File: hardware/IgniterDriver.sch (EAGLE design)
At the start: 51 parts, among them IC1 4066D, T3 TJ8S06M3L(T6L1,NQ)

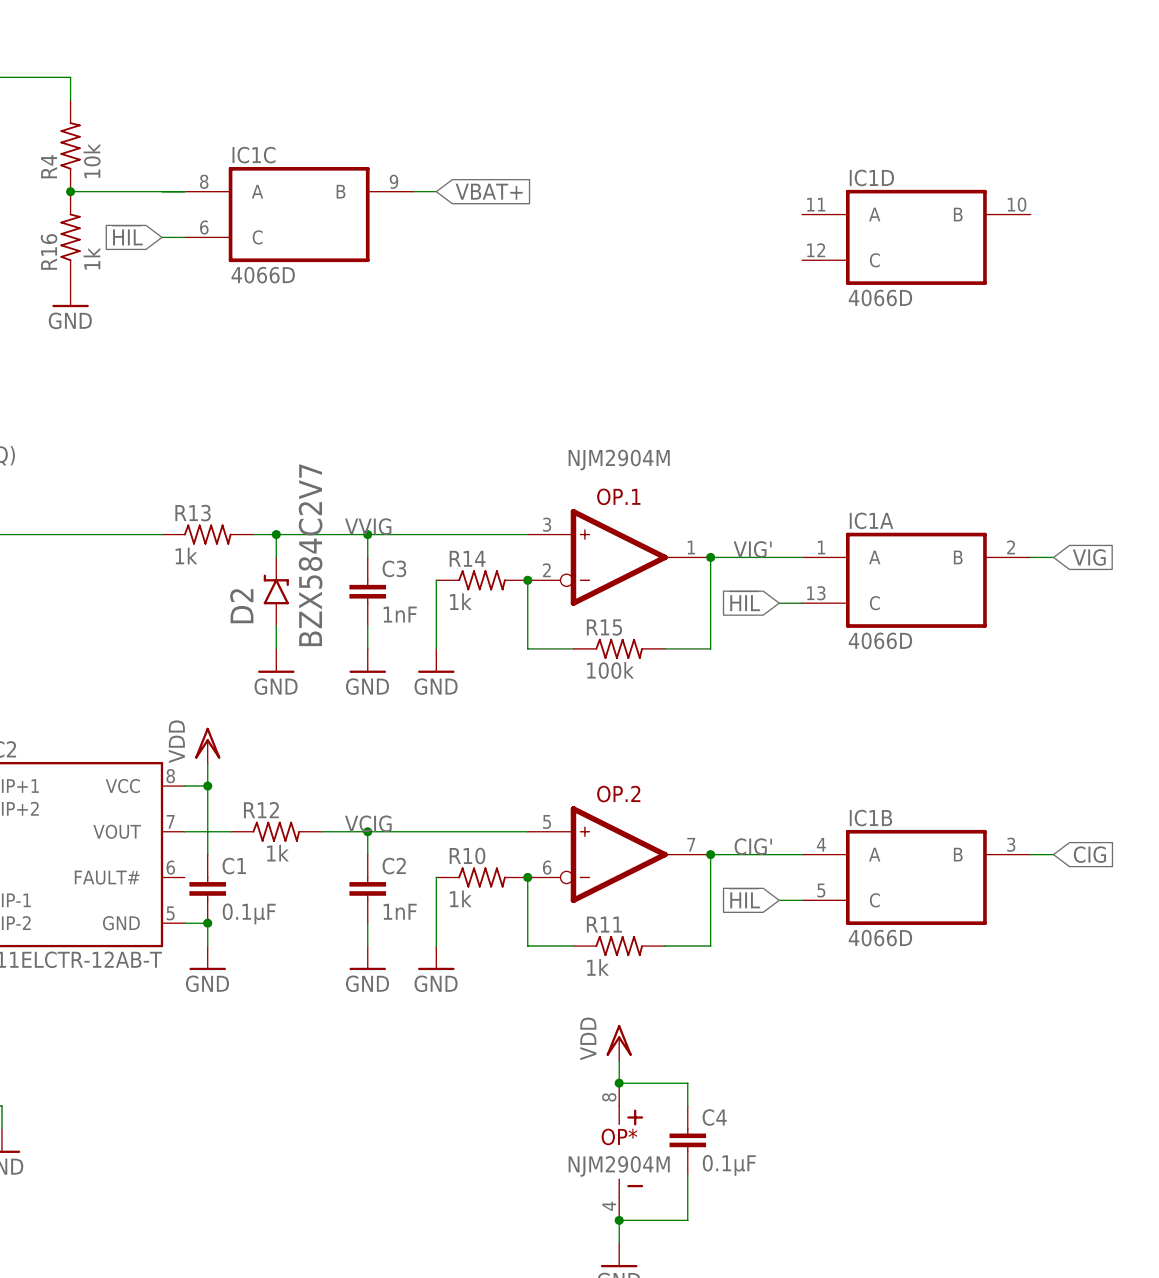
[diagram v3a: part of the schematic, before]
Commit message: Clean silk print
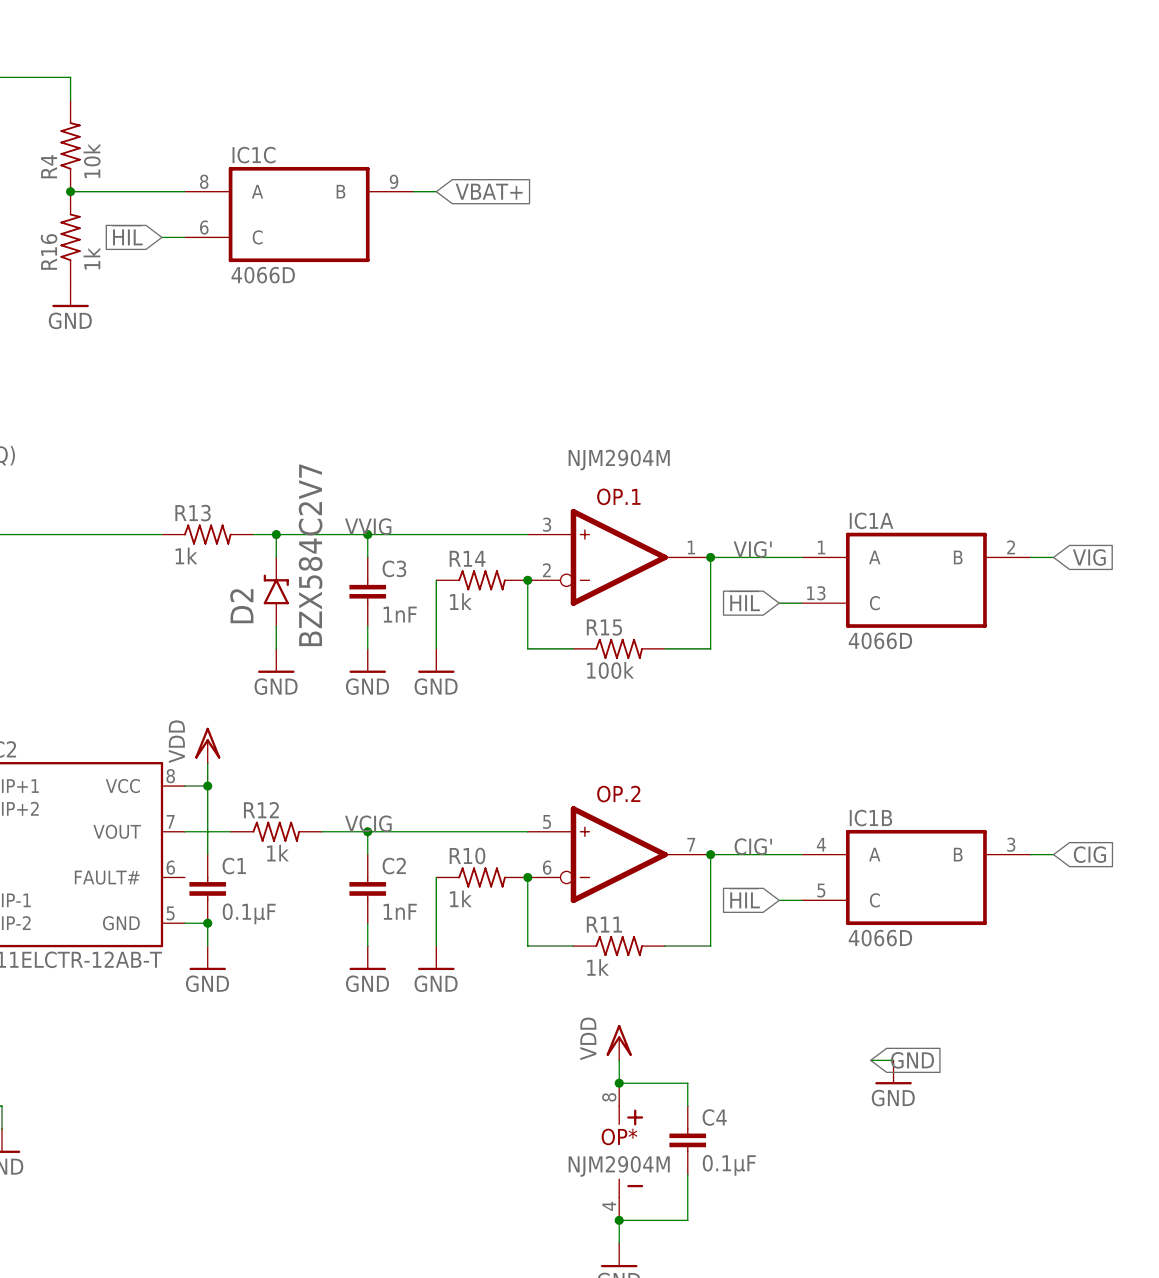
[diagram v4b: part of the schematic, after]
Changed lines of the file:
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@@
 <part name="R20" library="resistor" library_urn="urn:adsk.eagle:library:348" deviceset="R-US_" device="R0603" package3d_urn="urn:adsk.eagle:package:26057/1" value="1k"/>
 <part name="R21" library="resistor" library_urn="urn:adsk.eagle:library:348" deviceset="R-US_" device="R0603" package3d_urn="urn:adsk.eagle:package:26057/1" value="1k"/>
+<part name="GND20" library="supply1" library_urn="urn:adsk.eagle:library:371" deviceset="GND" device=""/>
 </parts>
 <sheets>
@@
 <attribute name="VALUE" x="193.04" y="152.4" size="1.778" layer="96"/>
 </instance>
-<instance part="IC1" gate="D" x="269.24" y="157.48" smashed="yes">
-<attribute name="NAME" x="261.62" y="163.195" size="1.778" layer="95"/>
-<attribute name="VALUE" x="261.62" y="149.86" size="1.778" layer="96"/>
-</instance>
 <instance part="C4" gate="G$1" x="243.84" y="58.42" smashed="yes">
 <attribute name="NAME" x="245.364" y="58.801" size="1.778" layer="95"/>
@@
 <attribute name="NAME" x="92.4814" y="179.07" size="1.778" layer="95" rot="R90"/>
 <attribute name="VALUE" x="92.202" y="191.77" size="1.778" layer="96" rot="R90"/>
+</instance>
+<instance part="GND20" gate="1" x="266.7" y="63.5" smashed="yes">
+<attribute name="VALUE" x="264.16" y="60.96" size="1.778" layer="96"/>
 </instance>
 </instances>
@@
 <pinref part="GND15" gate="1" pin="GND"/>
 </segment>
+<segment>
+<wire x1="264.16" y1="66.04" x2="266.7" y2="66.04" width="0.1524" layer="91"/>
+<pinref part="GND20" gate="1" pin="GND"/>
+<label x="264.16" y="66.04" size="1.778" layer="95" xref="yes"/>
+</segment>
 </net>
 <net name="VDD" class="0">
@@
 <junction x="175.26" y="162.56"/>
 <pinref part="IC1" gate="C" pin="A"/>
-<wire x1="187.96" y1="162.56" x2="185.42" y2="162.56" width="0.1524" layer="91"/>
-</segment>
-</net>
+</segment>
+</net>
